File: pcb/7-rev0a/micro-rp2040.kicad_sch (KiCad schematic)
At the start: 58 parts, among them J201 Conn_01x03, J202 TYPE-C-31-M-12, Q1 MMBT7002K, Q2 MMBT7002K, SW101 TS3425BA 098 2.5H 250gf, SW102 TS3315A 250gf 025, U1 RP2350B, U102 W25Q128JVSIQ, U105 MT29F1G01ABAFDWB, U3 TLV74311PDBVR, U401 ME6211A33PG-N, U8 APS6404L-3SQR-ZR, Y101 ABM8-272-T3

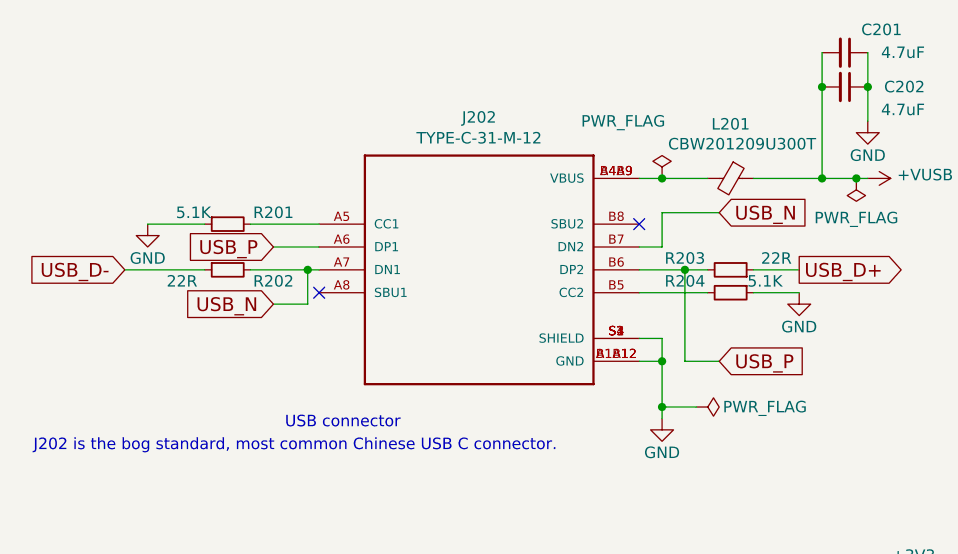
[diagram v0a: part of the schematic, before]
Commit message: change to 27R usb termination resistors as recommended by RasPi (7-rev0a)
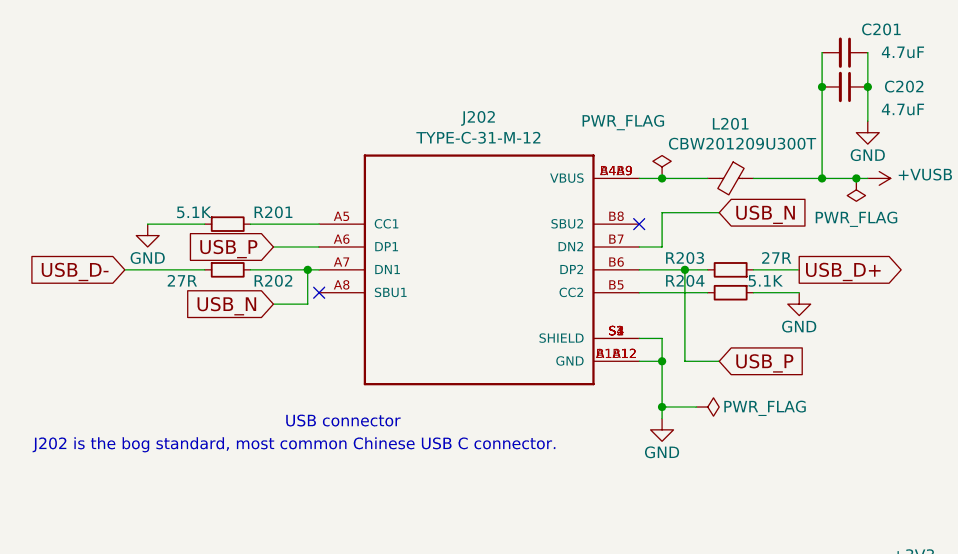
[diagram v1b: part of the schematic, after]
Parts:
- R202, R203: value 22R -> 27R
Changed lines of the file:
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@@
 			)
 		)
-		(property "Value" "22R"
+		(property "Value" "27R"
 			(at 39.37 48.26 90)
 			(effects
@@
 			)
 		)
-		(property "Value" "22R"
+		(property "Value" "27R"
 			(at 105.41 45.72 90)
 			(effects

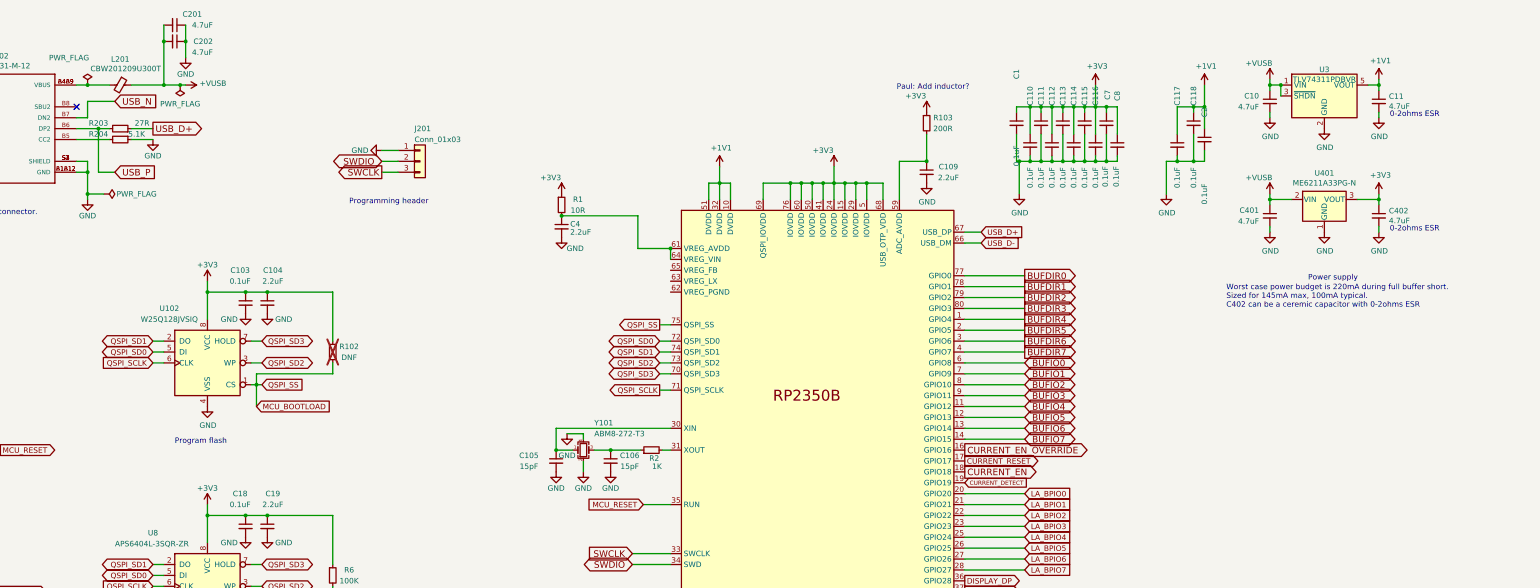
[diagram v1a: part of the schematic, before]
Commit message: BP7 REV 0a: 2.2uF, 4.7uF -> 10uF/6.3V CL05A106MQ5NUN
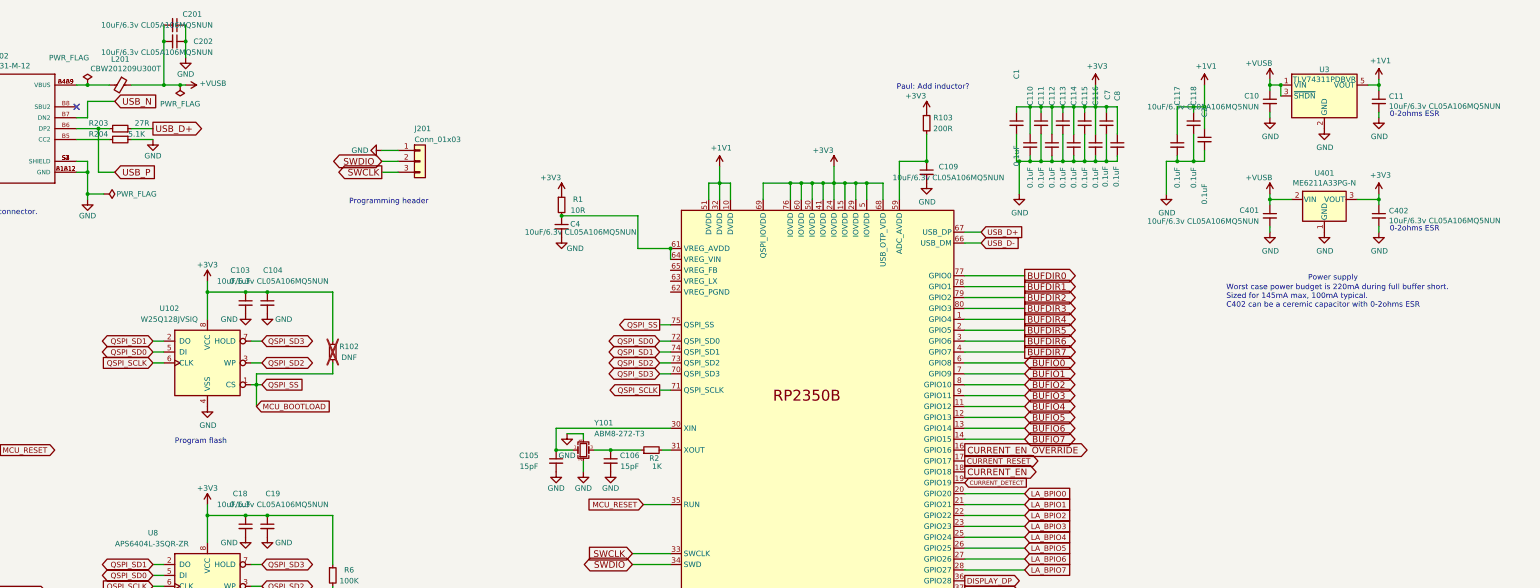
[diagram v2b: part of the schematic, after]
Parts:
- C10, C11, C201, C202, C401, C402: value 4.7uF -> 10uF/6.3v CL05A106MQ5NUN
- C104, C109, C19, C4: value 2.2uF -> 10uF/6.3v CL05A106MQ5NUN
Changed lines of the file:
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@@
 			)
 		)
-		(property "Value" "4.7uF"
+		(property "Value" "10uF/6.3v CL05A106MQ5NUN"
 			(at 365.76 68.58 0)
 			(effects
@@
 			)
 		)
-		(property "Value" "4.7uF"
+		(property "Value" "10uF/6.3v CL05A106MQ5NUN"
 			(at 396.0368 68.453 0)
 			(effects
@@
 			)
 		)
-		(property "Value" "4.7uF"
+		(property "Value" "10uF/6.3v CL05A106MQ5NUN"
 			(at 121.92 22.86 90)
 			(effects
@@
 			)
 		)
-		(property "Value" "4.7uF"
+		(property "Value" "10uF/6.3v CL05A106MQ5NUN"
 			(at 121.92 29.21 90)
 			(effects
@@
 			)
 		)
-		(property "Value" "2.2uF"
+		(property "Value" "10uF/6.3v CL05A106MQ5NUN"
 			(at 135.89 82.55 0)
 			(effects
@@
 			)
 		)
-		(property "Value" "2.2uF"
+		(property "Value" "10uF/6.3v CL05A106MQ5NUN"
 			(at 293.37 58.42 0)
 			(effects
@@
 			)
 		)
-		(property "Value" "2.2uF"
+		(property "Value" "10uF/6.3v CL05A106MQ5NUN"
 			(at 135.89 134.62 0)
 			(effects
@@
 			)
 		)
-		(property "Value" "4.7uF"
+		(property "Value" "10uF/6.3v CL05A106MQ5NUN"
 			(at 365.76 41.91 0)
 			(effects
@@
 			)
 		)
-		(property "Value" "2.2uF"
+		(property "Value" "10uF/6.3v CL05A106MQ5NUN"
 			(at 207.645 71.12 0)
 			(effects
@@
 			)
 		)
-		(property "Value" "4.7uF"
+		(property "Value" "10uF/6.3v CL05A106MQ5NUN"
 			(at 396.0368 41.783 0)
 			(effects

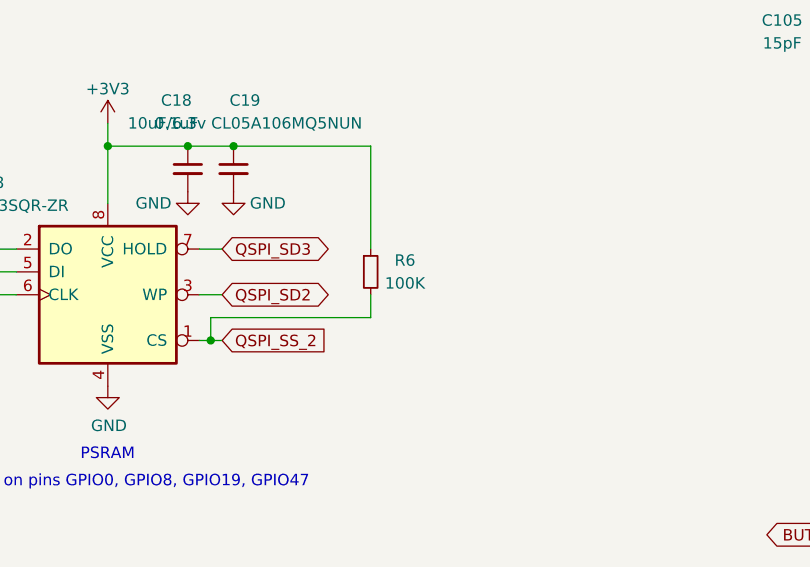
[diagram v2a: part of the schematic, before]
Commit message: PSRAM pullup to 10K
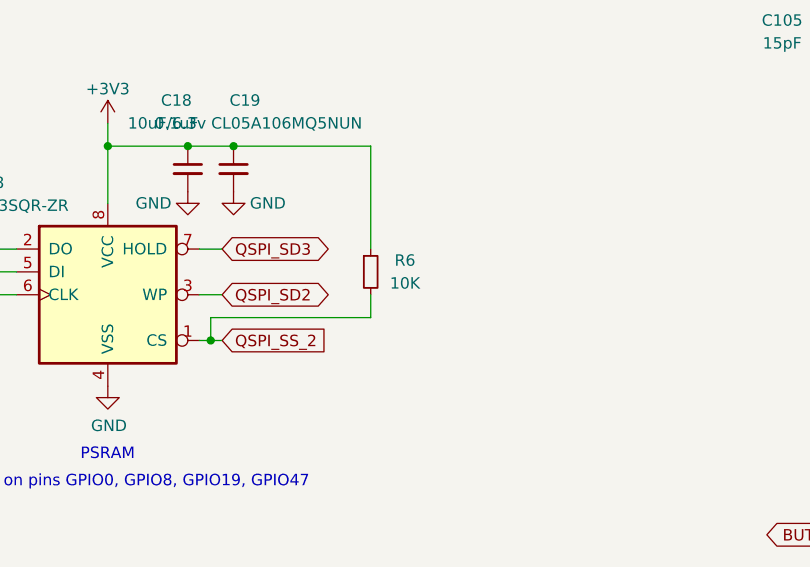
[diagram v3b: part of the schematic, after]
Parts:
- R6: value 100K -> 10K
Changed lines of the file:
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@@
 			)
 		)
-		(property "Value" "100K"
+		(property "Value" "10K"
 			(at 153.67 152.4 0)
 			(effects

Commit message: reorg, but forgot to check changes first :(
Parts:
- C21: value 10uF -> 10uF/6.3v CL05A106MQ5NUN
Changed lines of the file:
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@@
 			)
 		)
-		(property "Value" "10uF"
+		(property "Value" "10uF/6.3v CL05A106MQ5NUN"
 			(at 44.45 143.51 0)
 			(effects
